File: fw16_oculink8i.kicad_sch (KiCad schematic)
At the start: 21 parts, among them J1 FXBeam, J2 Fan0, J3 Fan1, J4 173162-0131, U1 BR24G32FVT-3GE2

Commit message: Remove FXBeam from BOM
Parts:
- J1: now left out of the parts list
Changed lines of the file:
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@@
 		(unit 1)
 		(exclude_from_sim no)
-		(in_bom yes)
+		(in_bom no)
 		(on_board yes)
 		(dnp no)

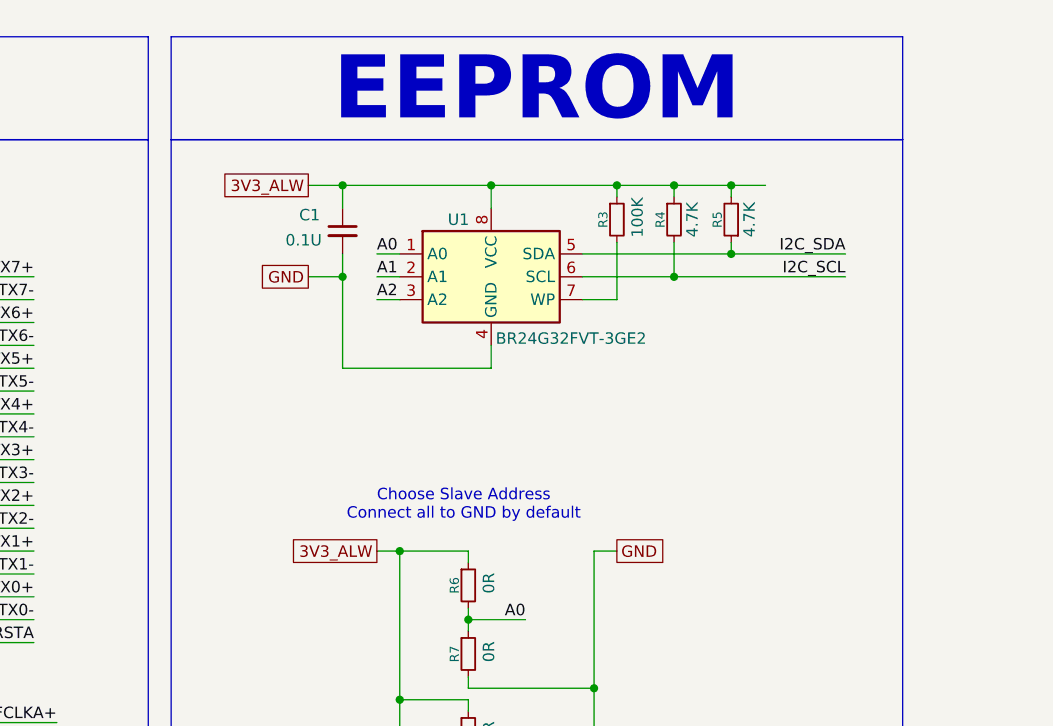
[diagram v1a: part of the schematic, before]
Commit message: Add R0 resistors to EEPROM power supply
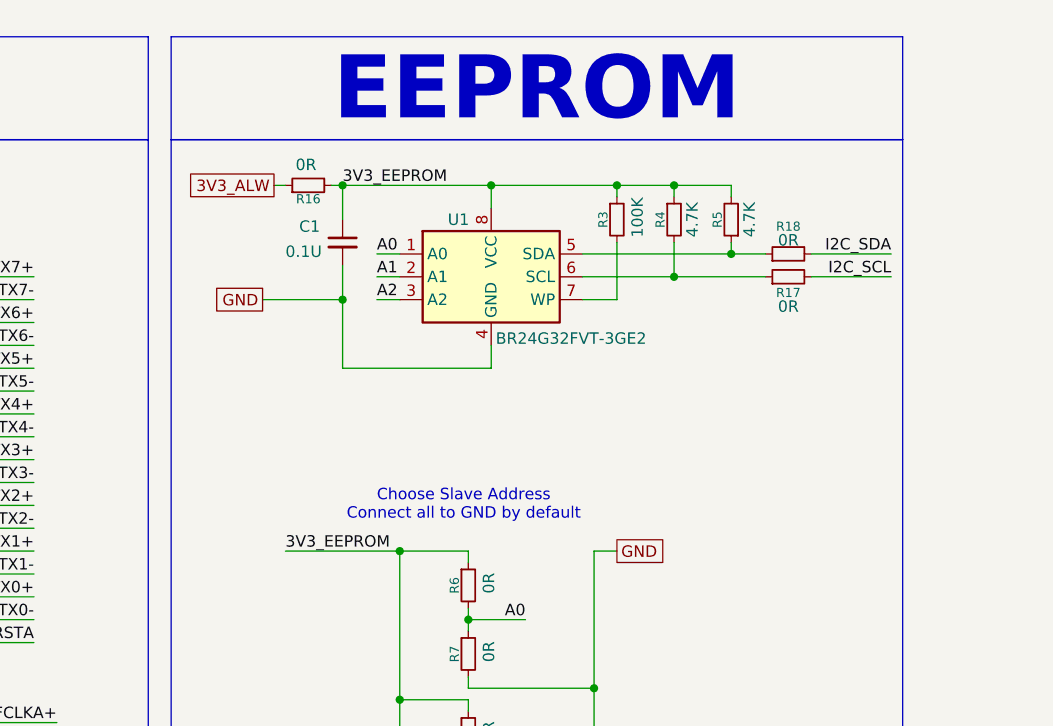
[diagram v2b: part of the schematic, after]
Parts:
- added R16, R17, R18: 0R, Resistor_SMD:R_0402_1005Metric, symbol Device:R_Small
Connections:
- net 3V3_ALW: now also R16.1; no longer C1.1, R10.1, R3.1, R4.1, R5.2, R6.1, R8.1, U1.8 (VCC)
- net I2C_SCL: now also R17.2; no longer R4.2, U1.6 (SCL)
- net I2C_SDA: now also R18.2; no longer R5.1, U1.5 (SDA)
- new net: R18.1, R5.1, U1.5 (SDA)
- new net: R17.1, R4.2, U1.6 (SCL)
- new net 3V3_EEPROM: C1.1, R10.1, R16.2, R3.1, R4.1, R5.2, R6.1, R8.1, U1.8 (VCC)
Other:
- moved on the sheet: C1

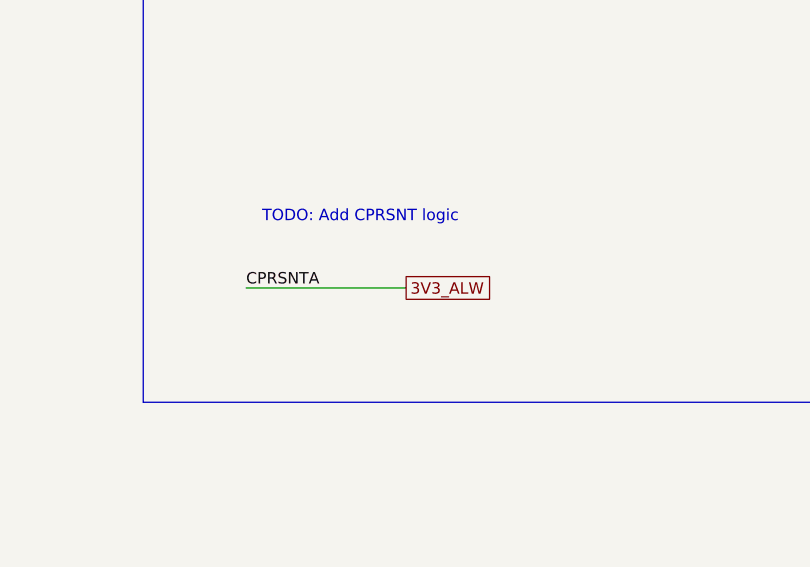
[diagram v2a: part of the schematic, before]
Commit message: Add R0 resistor to CPRSNT oculink pin
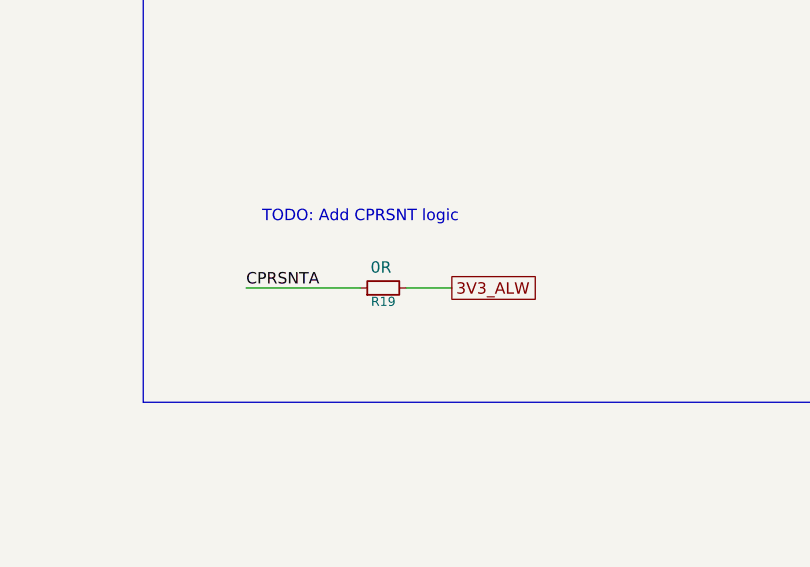
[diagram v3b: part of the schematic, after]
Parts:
- added R19: 0R, Resistor_SMD:R_0402_1005Metric, symbol Device:R_Small
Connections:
- net 3V3_ALW: now also R19.2; no longer J4.B12, R15.2
- new net CPRSNTA: J4.B12, R15.2, R19.1
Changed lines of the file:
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@@
 	(wire
 		(pts
-			(xy 297.18 238.76) (xy 314.96 238.76)
+			(xy 297.18 238.76) (xy 309.88 238.76)
 		)
 		(stroke
@@
 	(wire
 		(pts
+			(xy 314.96 238.76) (xy 320.04 238.76)
+		)
+		(stroke
+			(width 0)
+			(type default)
+		)
+	)
+	(wire
+		(pts
 			(xy 124.46 156.21) (xy 142.24 156.21)
 		)
@@
 	(global_label "3V3_ALW"
 		(shape passive)
-		(at 314.96 238.76 0)
+		(at 320.04 238.76 0)
 		(fields_autoplaced yes)
 		(effects
@@
 		)
 		(property "Intersheetrefs" "${INTERSHEET_REFS}"
-			(at 324.8772 238.76 0)
+			(at 329.9572 238.76 0)
 			(effects
 				(font
@@
 					(unit 1)
 				)
+			)
+		)
+	)
+	(symbol
+		(lib_id "Device:R_Small")
+		(at 312.42 238.76 90)
+		(unit 1)
+		(exclude_from_sim no)
+		(in_bom yes)
+		(on_board yes)
+		(dnp no)
+		(property "Reference" "R19"
+			(at 312.42 240.284 90)
+			(effects
+				(font
+					(size 1.016 1.016)
+				)
+			)
+		)
+		(property "Value" "0R"
+			(at 312.166 236.474 90)
+			(effects
+				(font
+					(size 1.27 1.27)
+				)
+			)
+		)
+		(property "Footprint" "Resistor_SMD:R_0402_1005Metric"
+			(at 312.42 238.76 0)
+			(effects
+				(font
+					(size 1.27 1.27)
+				)
+				(hide yes)
+			)
+		)
+		(property "Datasheet" "~"
+			(at 312.42 238.76 0)
+			(effects
+				(font
+					(size 1.27 1.27)
+				)
+				(hide yes)
+			)
+		)
+		(property "Description" "Resistor, small symbol"
+			(at 312.42 238.76 0)
+			(effects
+				(font
+					(size 1.27 1.27)
+				)
+				(hide yes)
+			)
+		)
+		(pin "2"
+		)
+		(pin "1"
+		)
+		(instances
+			(project "fw16_oculink8i"
+				(path "/50f5fd03-67f8-43d1-8bfe-dca2cf908bf0"
+					(reference "R19")
+					(unit 1)
+				)

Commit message: Remove unnecessary resistors from BOM
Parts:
- R10, R6, R8: now left out of the parts list
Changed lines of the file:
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@@
 		(unit 1)
 		(exclude_from_sim no)
-		(in_bom yes)
+		(in_bom no)
 		(on_board yes)
 		(dnp no)
@@
 		(unit 1)
 		(exclude_from_sim no)
-		(in_bom yes)
+		(in_bom no)
 		(on_board yes)
 		(dnp no)
@@
 		(unit 1)
 		(exclude_from_sim no)
-		(in_bom yes)
+		(in_bom no)
 		(on_board yes)
 		(dnp no)

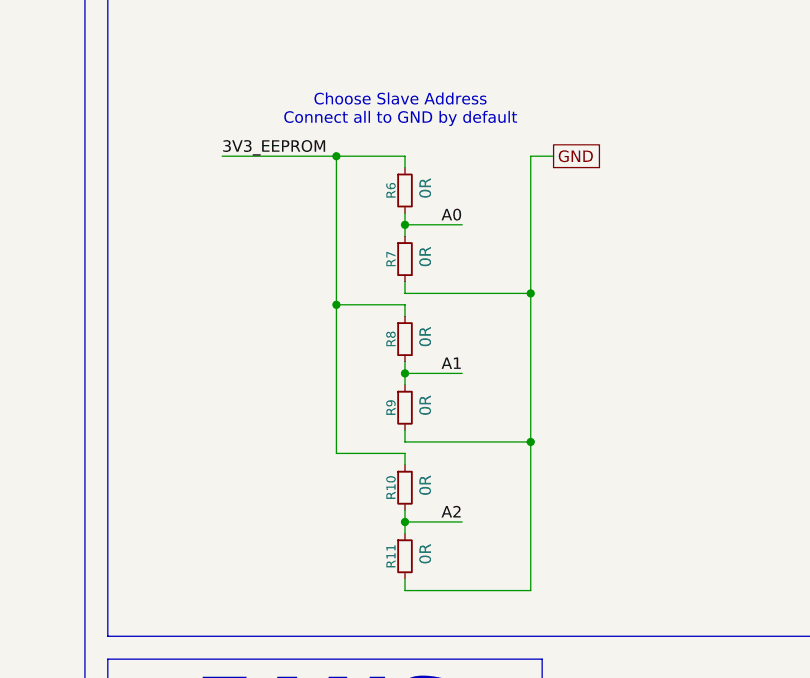
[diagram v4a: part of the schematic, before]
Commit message: Create separate nano-pitch footprint with JLC DRC rules
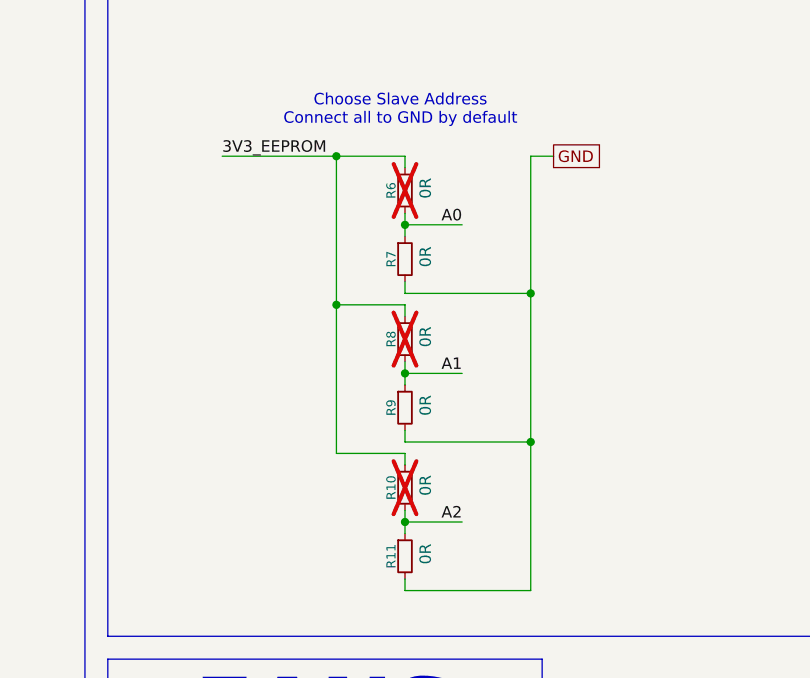
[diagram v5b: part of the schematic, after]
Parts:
- J4: footprint Nano_Pitch:Nano-Pitch-173162-0131 -> Nano_Pitch:Nano-Pitch-173162-0131_JLC-DRC
- R10, R6, R8: now not fitted; now in the parts list
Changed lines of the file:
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@@
 		(unit 1)
 		(exclude_from_sim no)
-		(in_bom no)
+		(in_bom yes)
 		(on_board yes)
-		(dnp no)
+		(dnp yes)
 		(property "Reference" "R6"
 			(at 130.556 77.47 90)
@@
 			)
 		)
-		(property "Footprint" "Nano_Pitch:Nano-Pitch-173162-0131"
+		(property "Footprint" "Nano_Pitch:Nano-Pitch-173162-0131_JLC-DRC"
 			(at 354.33 146.99 0)
 			(effects
@@
 		(unit 1)
 		(exclude_from_sim no)
-		(in_bom no)
+		(in_bom yes)
 		(on_board yes)
-		(dnp no)
+		(dnp yes)
 		(property "Reference" "R10"
 			(at 130.556 110.49 90)
@@
 		(unit 1)
 		(exclude_from_sim no)
-		(in_bom no)
+		(in_bom yes)
 		(on_board yes)
-		(dnp no)
+		(dnp yes)
 		(property "Reference" "R8"
 			(at 130.556 93.98 90)

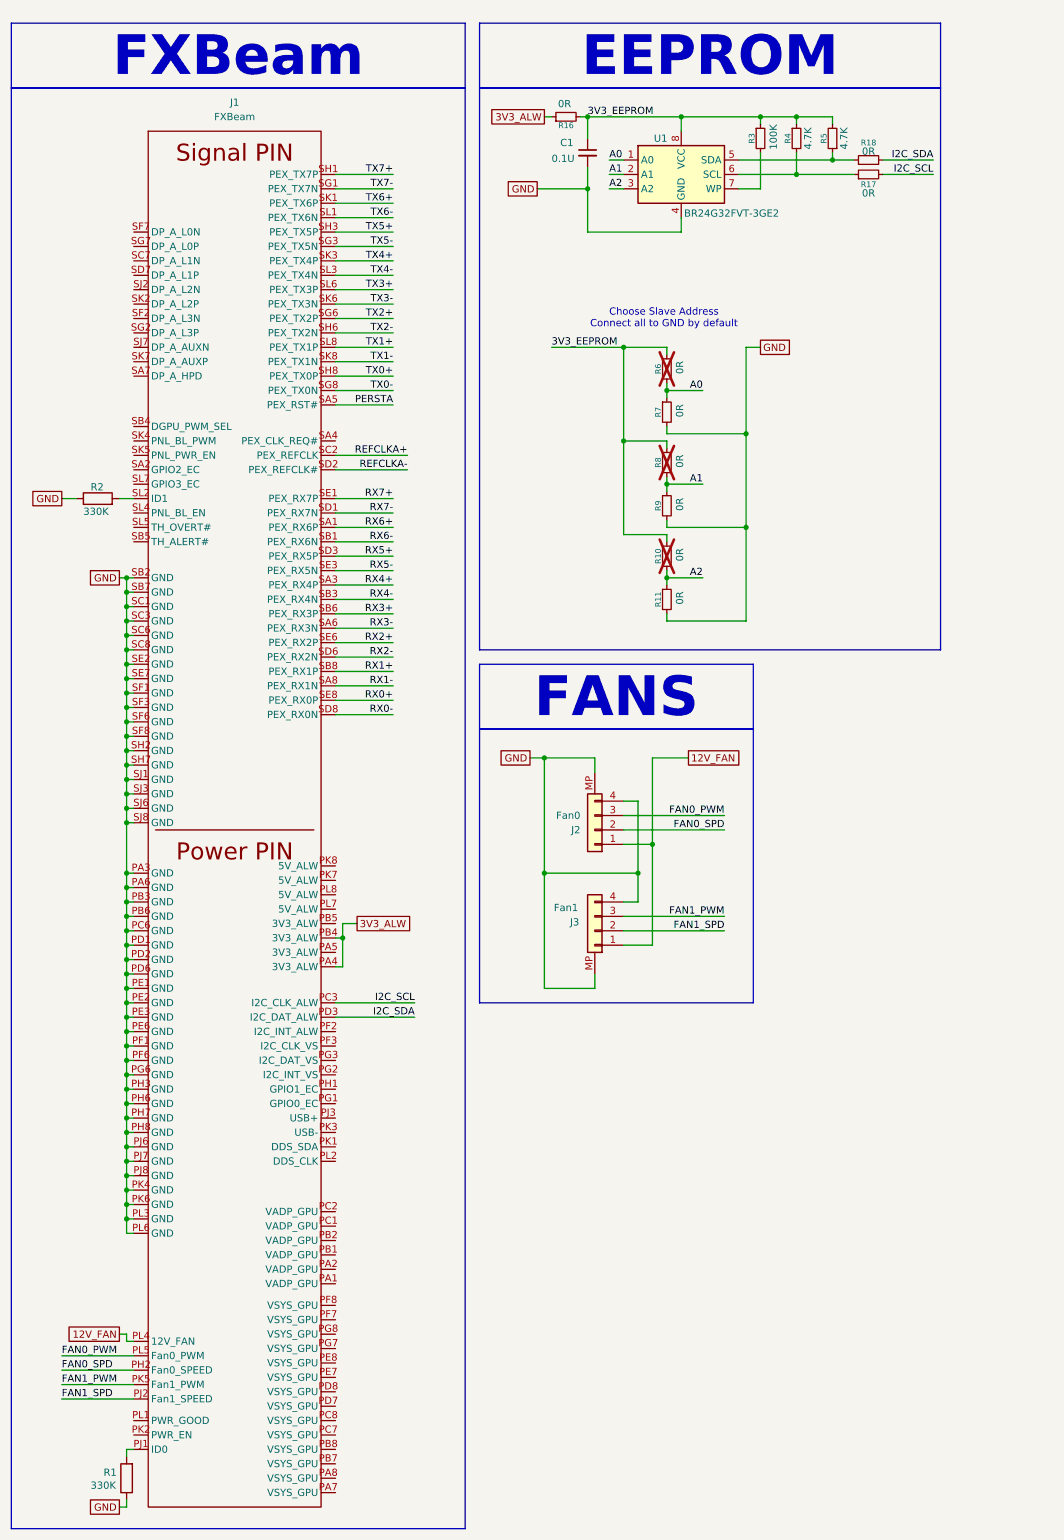
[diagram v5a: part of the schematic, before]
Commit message: Add CLKREQ trace and GND EEPROM WP resistor
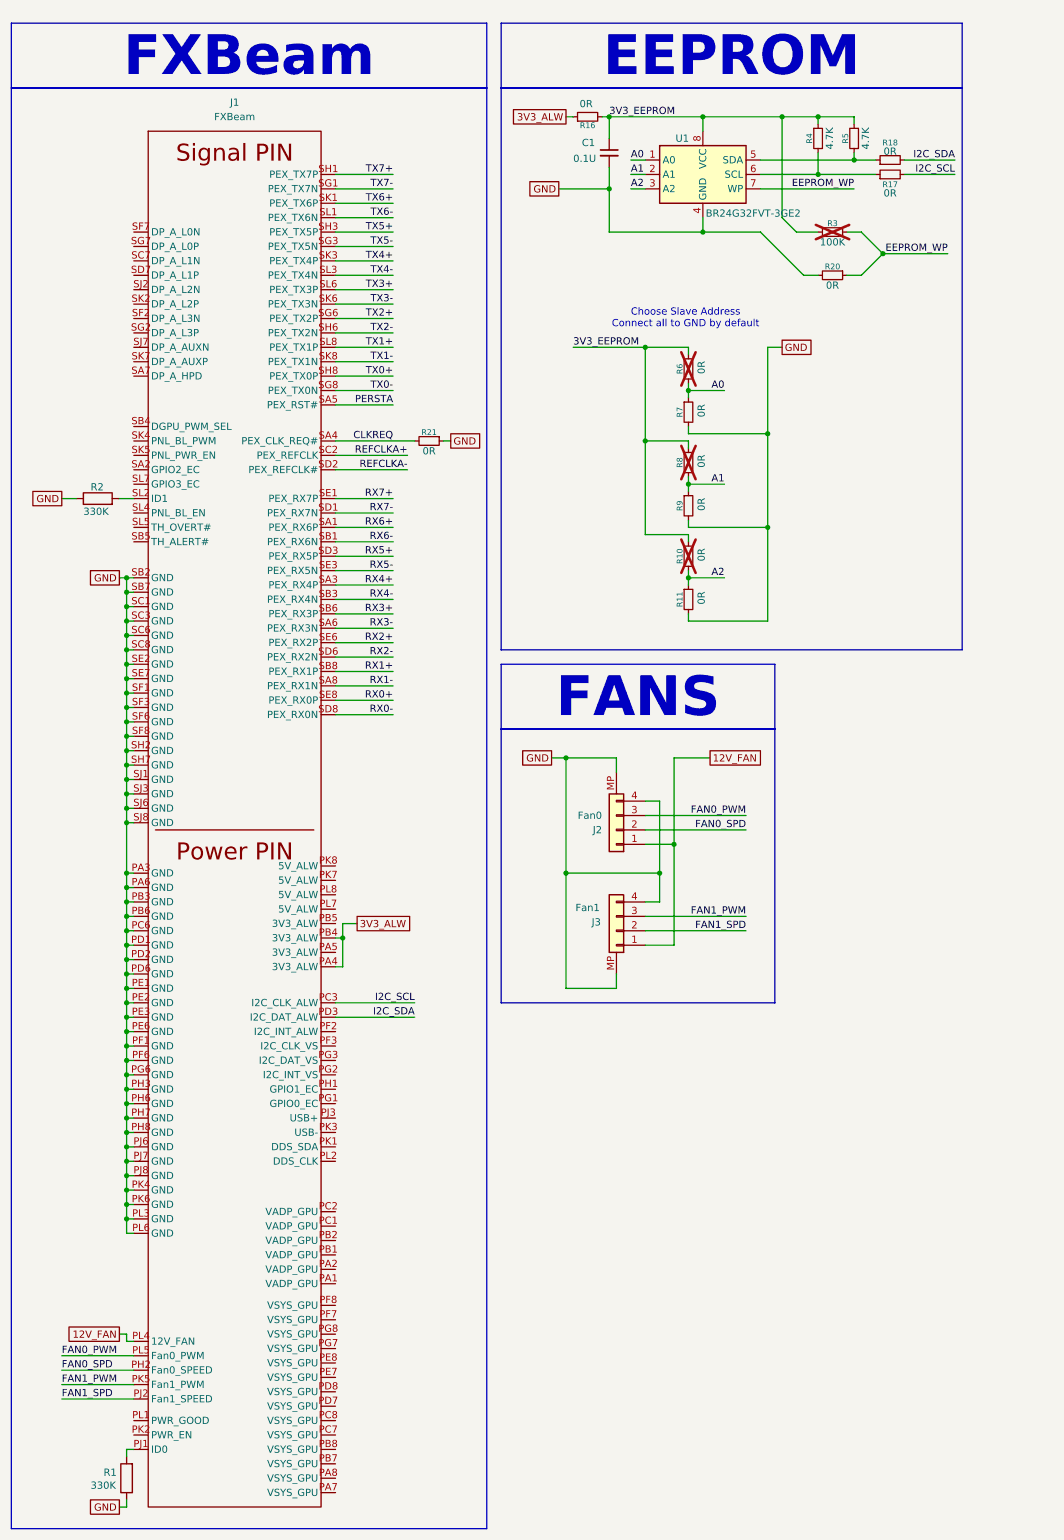
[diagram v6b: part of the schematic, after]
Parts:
- added R20, R21: 0R, Resistor_SMD:R_0402_1005Metric, symbol Device:R_Small
- R3: now not fitted
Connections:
- net 3V3_EEPROM: now also R3.2; no longer R3.1
- net GND: now also R20.2, R21.1
- net EEPROM_WP: now reaches U1.7 (WP)
- net EEPROM_WP: now also R3.1, R20.1; no longer R3.2
- net CLKREQ: now reaches J1.SA4 (PEX_CLK_REQ#)
- net CLKREQ: now also R21.2
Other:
- moved on the sheet: C1, J2, J3, R10, R11, R16, R17, R18, R4, R5, R6, R7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

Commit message: Finalize rev 1.1
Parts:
- removed R14, R15: 0R, Resistor_SMD:R_0402_1005Metric, symbol Device:R_Small
- added H1, H2, H3, H4: MountingHole_Pad, Expansion_Bay:MountingHole_6.2mm, symbol Mechanical:MountingHole_Pad
- added R14, R15, R22, R23: 0R, Resistor_SMD:R_0402_1005Metric, symbol Device:R
- added TP1, TP2: TestPoint, TestPoint:TestPoint_Pad_D1.0mm, symbol Connector:TestPoint
- R12: value 0R -> R; now not fitted
- R13: value 0R -> 1K
- R19: value 0R -> 100K
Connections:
- net 3V3_ALW: now also R12.2
- net GND: now also R13.2, H1.1, H2.1, H3.1, H4.1; no longer R21.1
- net PERSTA: now also R14.2, R15.2, R22.2, R23.2; no longer J1.SA5 (PEX_RST#)
- net REFCLKA+: now also J1.SD2 (PEX_REFCLK#); no longer J1.SC2 (PEX_REFCLK), R12.1
- net REFCLKA-: now also J1.SC2 (PEX_REFCLK); no longer J1.SD2 (PEX_REFCLK#), R13.1
- net REFCLKB+: no longer R12.2
- net REFCLKB-: no longer R13.2
- net RX0+: now also J4.A3; no longer J4.A2
- net RX0-: now also J4.A2; no longer J4.A3
- net RX3+: now also J4.A18; no longer J4.A17
- net RX3-: now also J4.A17; no longer J4.A18
- net RX4+: now also J4.A24; no longer J4.A23
- net RX4-: now also J4.A23; no longer J4.A24
- net RX6+: now also J4.A36; no longer J4.A35
- net RX6-: now also J4.A35; no longer J4.A36
- net RX7+: now also J4.A39; no longer J4.A38
- net RX7-: now also J4.A38; no longer J4.A39
- net TX0+: now also J4.B3; no longer J4.B2
- net TX0-: now also J4.B2; no longer J4.B3
- net TX1+: now also J4.B6; no longer J4.B5
- net TX1-: now also J4.B5; no longer J4.B6
- net TX3+: now also J4.B18; no longer J4.B17
- net TX3-: now also J4.B17; no longer J4.B18
- net TX4+: now also J4.B24; no longer J4.B23
- net TX4-: now also J4.B23; no longer J4.B24
- net TX6+: now also J4.B36; no longer J4.B35
- net TX6-: now also J4.B35; no longer J4.B36
- net SSD1_RST: now reaches J1.PF3 (I2C_CLK_VS)
- net SSD1_RST: now also R14.1
- net at J1.PG1 (GPIO0_EC): now also TP1.1
- net SSD2_CLKREQ: now reaches J1.PG2 (I2C_INT_VS)
- net SSD2_CLKREQ: now also R22.1
- net SSD2_RST: now reaches J1.PG3 (I2C_DAT_VS)
- net SSD2_RST: now also R15.1
- net at J1.PH1 (GPIO1_EC): now also TP2.1
- new net: R12.1, R13.1, R21.1
- new net: J1.SA5 (PEX_RST#), R23.1
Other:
- moved on the sheet: C1, J2, J3, R10, R11, R16, R17, R18, R20, R21, R3, R4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
